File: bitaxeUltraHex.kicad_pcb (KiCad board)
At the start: 4 copper layers, 136.3 x 79.7 mm, 277 parts, among them J1 Conn_01x01, J2 Conn_01x01, J3 Conn_01x04, J4 TC2030-IDC, J5 Conn_01x04, J6 Conn_01x04, Q1 NTMFS5C673NLT1G, Q2 CSD17577Q5A, Q3 NTMFS5C673NLT1G, Q4 CSD17577Q5A, SW1 GT-TC029B-H025-L1N, SW2 GT-TC029B-H025-L1N, U1 uA7805, U10 25MHz, U11 BM1366_mode1, U12 TLV752, U13 MCP1824T-0802E, U14 BM1366_mode1, U15 TMP1075, U16 TMP1075, U17 EMC2302, U18 EMC2101, U19 TLV752, U2 RT9080-33GJ5, U20 MCP1824T-0802E, U21 BM1366_mode1, U22 BM1366_mode1, U23 TLV752, U24 MCP1824T-0802E, U25 BM1366_mode1, U26 BM1366_mode1, U3 INA219AIDCNR, U4 TPS40305, U5 DS4432U+, U6 SN74LVC1T45DBVR, U7 SN74LVC1T45DBVR, U8 SN74LVC1T45DBVR, U9 ESP32-S3-WROOM-1, Y1 32.768kHz

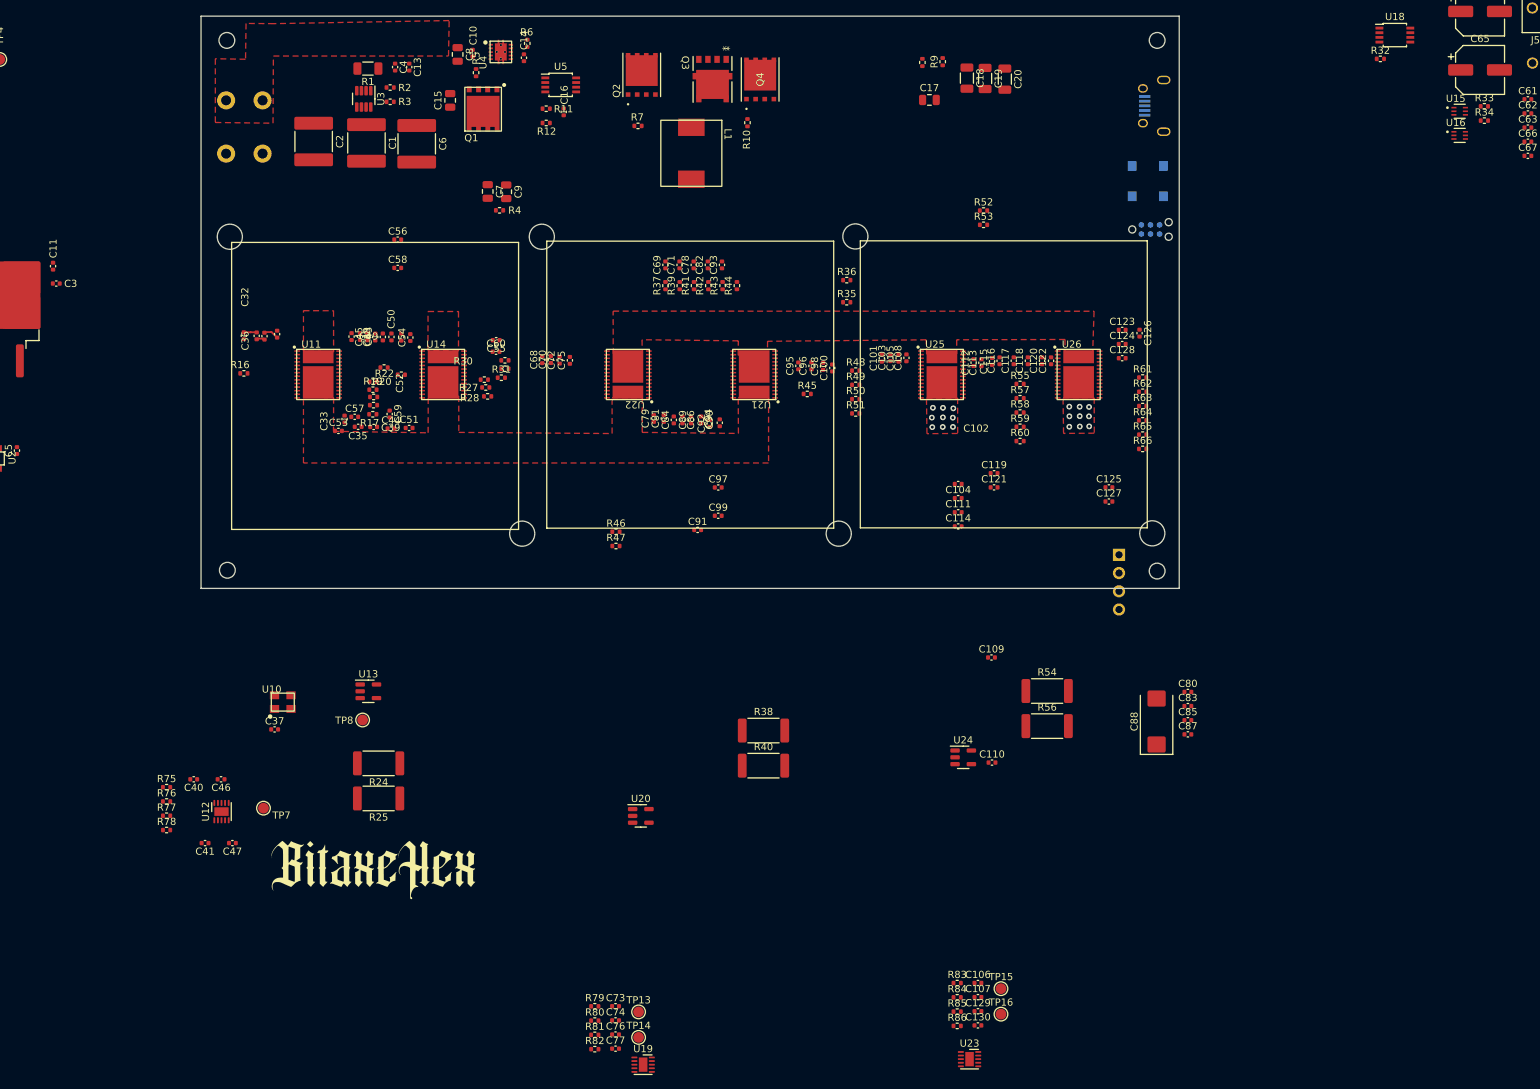
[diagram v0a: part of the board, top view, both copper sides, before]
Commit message: switch voltage reference regulators to ADP170, reannotate
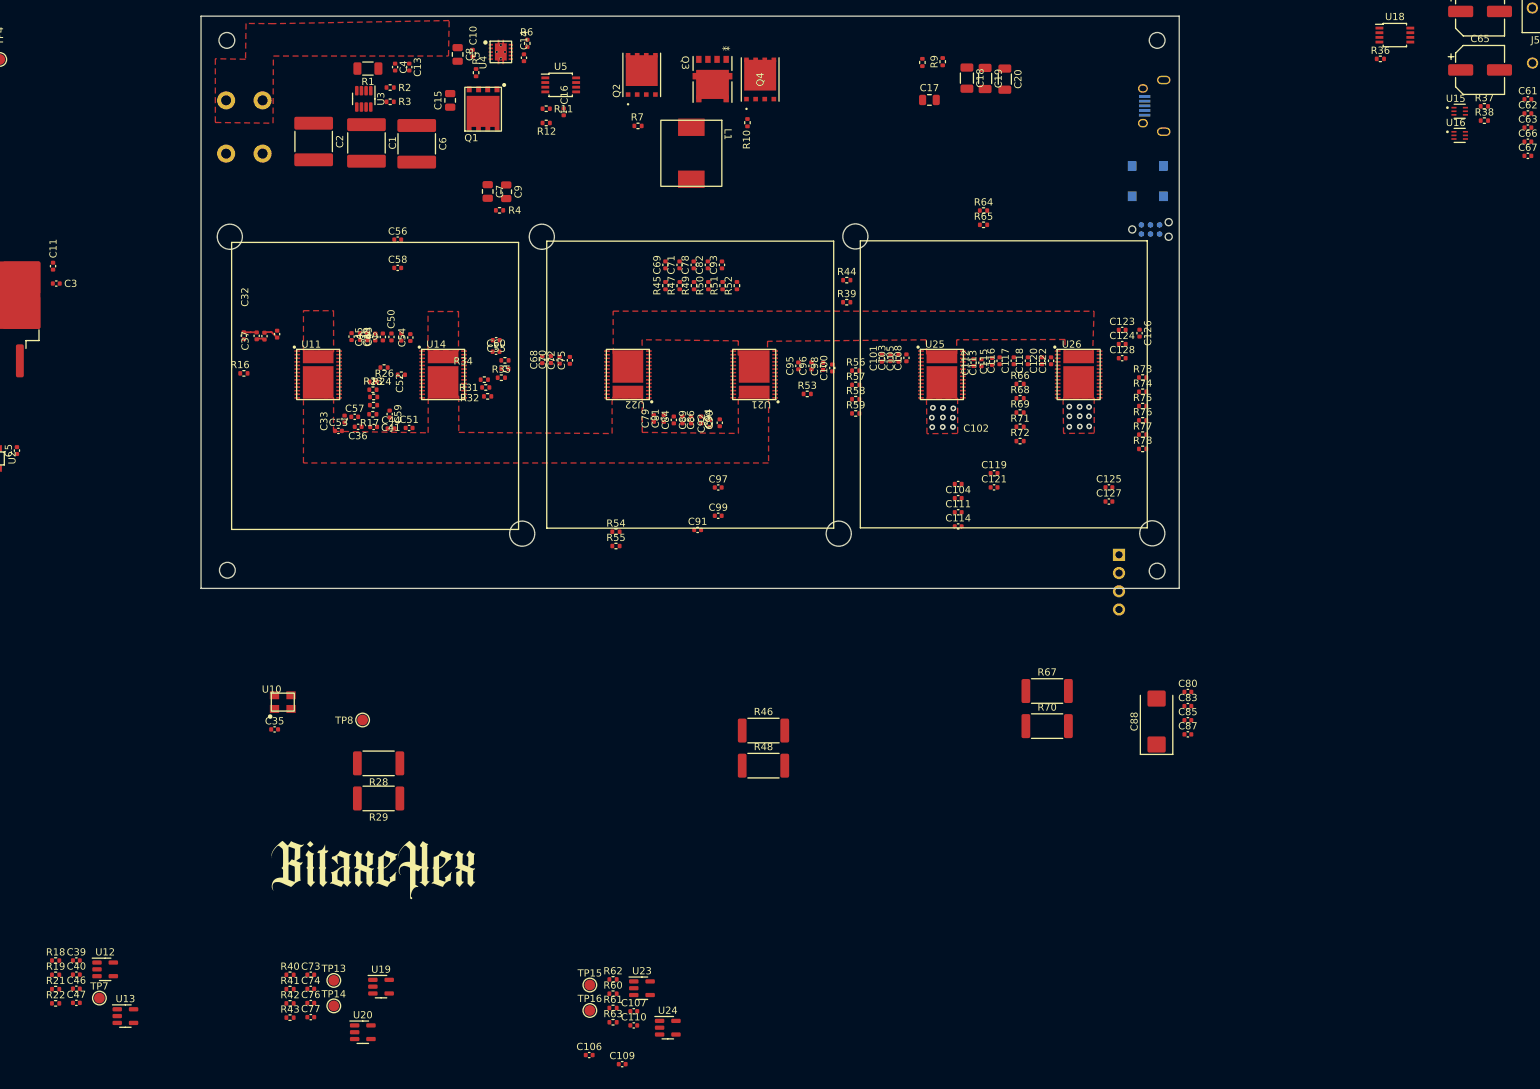
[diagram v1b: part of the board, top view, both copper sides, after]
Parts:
- removed the C106 at (161.8, 182.1)
- removed C129: 0.1uF, Capacitor_SMD:C_0402_1005Metric
- removed C130: 1uF, Capacitor_SMD:C_0402_1005Metric
- removed the C41 at (54.1, 162.6)
- removed the R75 at (48.7, 154.8)
- removed the R76 at (48.7, 156.8)
- removed the R77 at (48.7, 158.8)
- removed the R78 at (48.7, 160.7)
- removed R79, R83: 243K, Resistor_SMD:R_0402_1005Metric
- removed R80, R82, R84, R86: 536K, Resistor_SMD:R_0402_1005Metric
- removed R81, R85: 634K, Resistor_SMD:R_0402_1005Metric
- added C110: 1uF, Capacitor_SMD:C_0402_1005Metric, F.Cu at (113.8, 188.0)
- added C39: 0.1uF, Capacitor_SMD:C_0402_1005Metric, F.Cu at (36.2, 178.9)
- added R18: 309K, Resistor_SMD:R_0402_1005Metric, F.Cu at (33.3, 178.9)
- added R19: 130K, Resistor_SMD:R_0402_1005Metric, F.Cu at (33.3, 180.9)
- added R21: 182K, Resistor_SMD:R_0402_1005Metric, F.Cu at (33.3, 182.9)
- added R22: 182K, Resistor_SMD:R_0402_1005Metric, F.Cu at (33.3, 184.9)
- added R40: 309K, Resistor_SMD:R_0402_1005Metric, F.Cu at (65.9, 180.9)
- added R41: 130K, Resistor_SMD:R_0402_1005Metric, F.Cu at (65.9, 182.9)
- added R42: 182K, Resistor_SMD:R_0402_1005Metric, F.Cu at (65.9, 184.9)
- added R43: 182K, Resistor_SMD:R_0402_1005Metric, F.Cu at (65.9, 186.9)
- added R60: 309K, Resistor_SMD:R_0402_1005Metric, F.Cu at (110.9, 183.5)
- added R61: 130K, Resistor_SMD:R_0402_1005Metric, F.Cu at (110.9, 185.5)
- added R62: 182K, Resistor_SMD:R_0402_1005Metric, F.Cu at (110.9, 181.6)
- added R63: 182K, Resistor_SMD:R_0402_1005Metric, F.Cu at (110.9, 187.5)
- C106: renamed from C110; value 1uF -> 0.1uF
- C107: value 1uF -> 0.1uF
- U12, U19, U23: value TLV752 -> ADP171AUJ-R7; footprint Package_SON:WSON-10-1EP_2.5x2.5mm_P0.5mm_EP1.2x2mm -> Package_TO_SOT_SMD:TSOT-23-5
- U13: renamed from U24; value MCP1824T-0802E -> ADP171AUJ-R7; footprint Package_TO_SOT_SMD:SOT-23-5 -> Package_TO_SOT_SMD:TSOT-23-5
- U20: value MCP1824T-0802E -> ADP171AUJ-R7; footprint Package_TO_SOT_SMD:SOT-23-5 -> Package_TO_SOT_SMD:TSOT-23-5
- U24: renamed from U13; value MCP1824T-0802E -> ADP171AUJ-R7; footprint Package_TO_SOT_SMD:SOT-23-5 -> Package_TO_SOT_SMD:TSOT-23-5
- moved U13 122.2 mm to (43.0, 186.7)
- moved C109 76.5 mm to (112.2, 193.4)
- moved C106 69.4 mm to (107.6, 192.1)
- moved U24 62.7 mm to (118.6, 188.3)
- moved TP15 57.3 mm to (107.7, 182.3)
- moved TP16 57.3 mm to (107.7, 185.9)
- moved U20 49.1 mm to (76.1, 188.9)
- moved C107 48.0 mm to (113.8, 186.0)
- moved U23 46.7 mm to (115.0, 182.8)
- moved C73 42.7 mm to (68.8, 180.9)
- moved C74 42.7 mm to (68.8, 182.9)
- moved C76 42.7 mm to (68.8, 184.8)
- moved C77 42.7 mm to (68.8, 186.8)
- moved TP13 42.7 mm to (72.0, 181.7)
- moved TP14 42.7 mm to (72.0, 185.2)
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- renumbered C37 to C35, C35 to C36, C36 to C37, C39 to C41, R18 to R20, R19 to R23, R20 to R24, R21 to R25, R22 to R26, R23 to R27, R24 to R28, R25 to R29, R26 to R30, R27 to R31, R28 to R32, R29 to R33, R30 to R34, R31 to R35, R32 to R36, R33 to R37, R34 to R38, R35 to R39, R36 to R44, R37 to R45, R38 to R46, R39 to R47, R40 to R48, R41 to R49, R42 to R50, R43 to R51, R44 to R52, R45 to R53, R46 to R54, R47 to R55, R48 to R56, R49 to R57, R50 to R58, R51 to R59, R52 to R64, R53 to R65, R55 to R66, R54 to R67, R57 to R68, R58 to R69, R56 to R70, R59 to R71, R60 to R72, R61 to R73, R62 to R74, R63 to R75, R64 to R76, R65 to R77, R66 to R78
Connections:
- C106 pad 1: /BM1366-3/0V8 -> /5V
- C107 pad 1: /BM1366-3/1V2 -> /5V
- C109 pad 1: /BM1366-3/1V2 -> /BM1366-3/0V8
- U12 pad 1: Net-(U12A-FB1) -> /5V
- U12 pad 4: /FGND2 -> Net-(U12-ADJ)
- U12 pad 5: /5V -> /BM1366-1/0V8
- U13 pad 2: GND -> /FGND2
- U13 pad 4: unconnected-(U24-PG-Pad4) -> Net-(U13-ADJ)
- U13 pad 5: /BM1366-3/0V8 -> /BM1366-1/1V2
- U19 pad 1: Net-(U19A-FB1) -> /5V
- U19 pad 4: /FGND1 -> Net-(U19-ADJ)
- U19 pad 5: /5V -> /BM1366-2/0V8
- U20 pad 2: /BM1366-2/GND -> /FGND1
- U20 pad 4: unconnected-(U20-PG-Pad4) -> Net-(U20-ADJ)
- U20 pad 5: /BM1366-2/0V8 -> /BM1366-2/1V2
- U23 pad 1: Net-(U23A-FB1) -> /5V
- U23 pad 4: GND -> Net-(U23-ADJ)
- U23 pad 5: /5V -> /BM1366-3/0V8
- U24 pad 2: /BM1366-1/GND -> GND
- U24 pad 4: unconnected-(U13-PG-Pad4) -> Net-(U24-ADJ)
- U24 pad 5: /BM1366-1/0V8 -> /BM1366-3/1V2

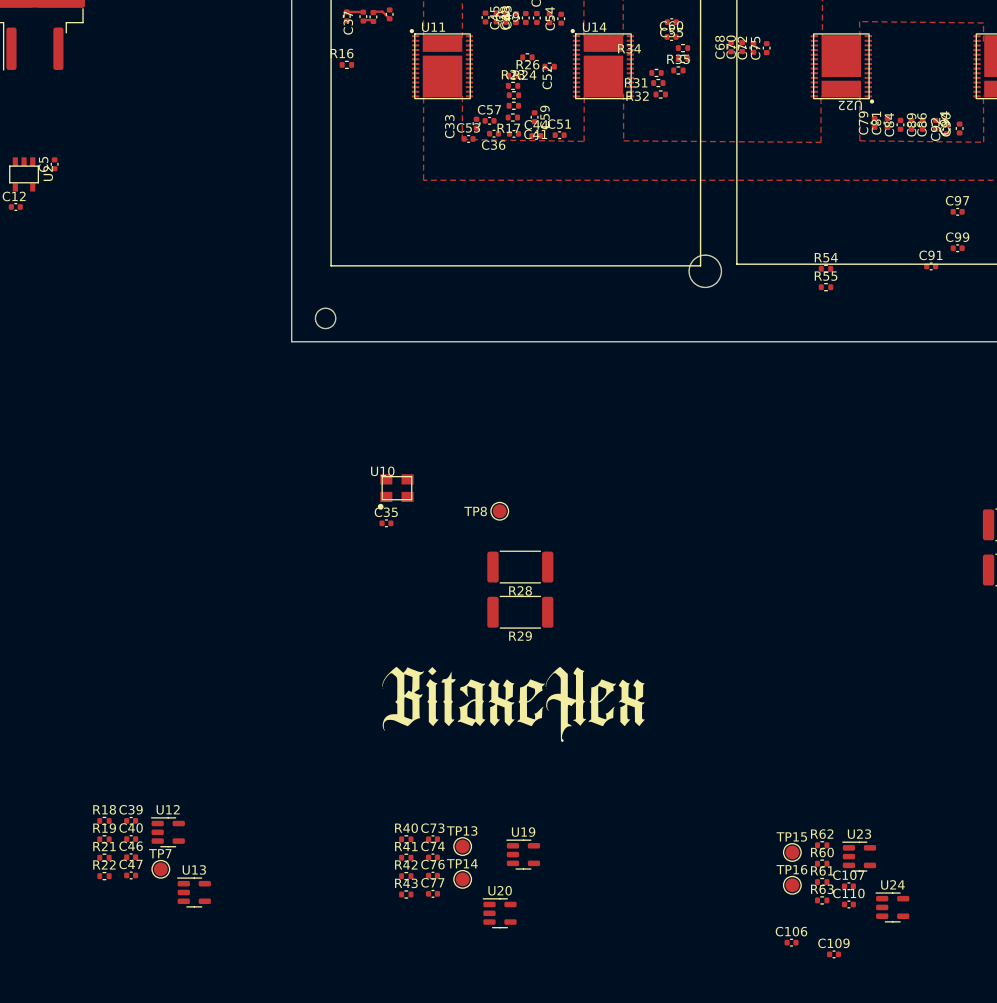
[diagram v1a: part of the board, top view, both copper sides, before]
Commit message: arrange components around voltage regulators
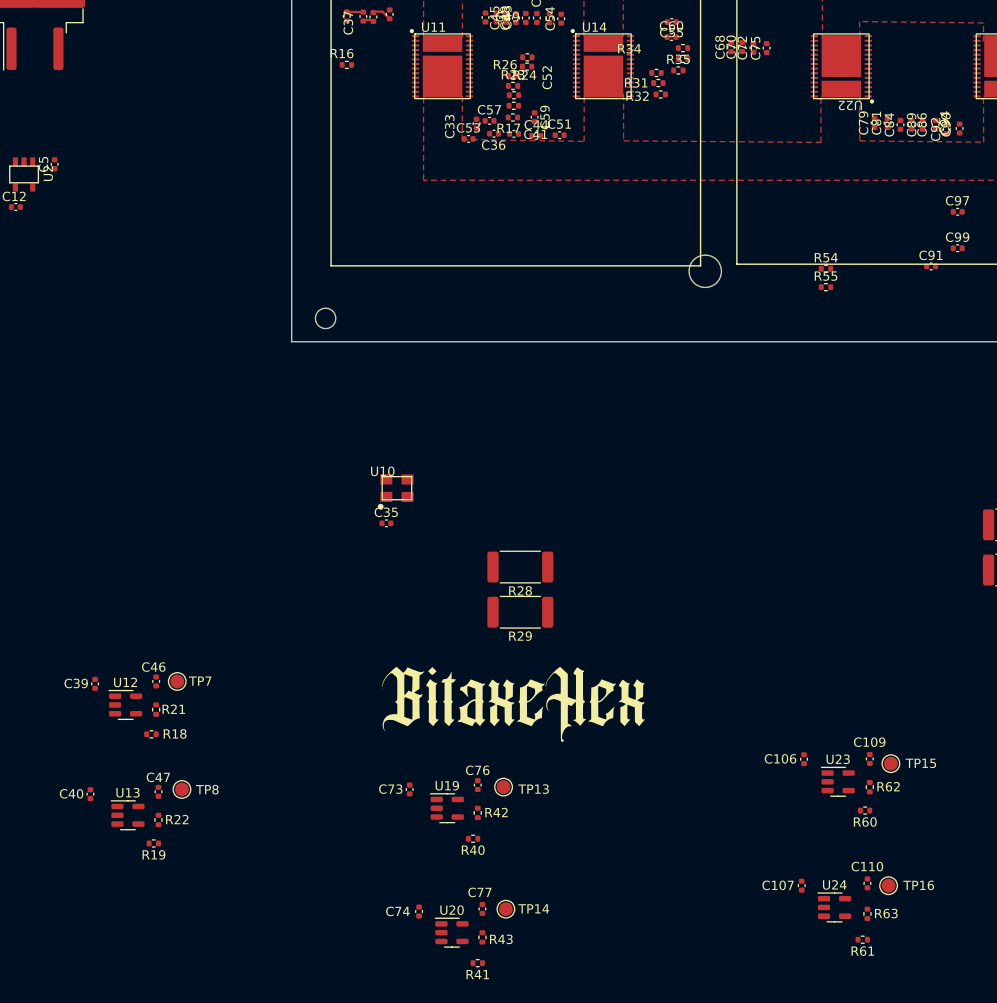
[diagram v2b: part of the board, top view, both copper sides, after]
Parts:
- moved TP8 45.7 mm to (41.7, 175.5)
- moved C109 21.5 mm to (116.1, 172.2), turned to 90 degrees
- moved TP7 20.4 mm to (41.1, 163.8)
- moved C106 19.9 mm to (109.0, 172.2), turned to 90 degrees
- moved C46 19.2 mm to (38.9, 163.8), turned to 90 degrees
- moved R21 17.0 mm to (38.9, 166.9), turned to -90 degrees
- moved C39 15.3 mm to (32.3, 164.1), turned to 90 degrees
- moved U12 14.5 mm to (35.6, 166.4)
- moved TP15 14.4 mm to (118.4, 172.7)
- moved R41 13.8 mm to (73.7, 194.3)
- moved U13 11.0 mm to (35.8, 178.3)
- moved C76 10.9 mm to (73.7, 175.0), turned to 90 degrees
- moved R18 10.7 mm to (38.4, 169.5)
- moved TP16 10.4 mm to (118.1, 185.9)
- moved R42 10.3 mm to (73.7, 178.1), turned to -90 degrees
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
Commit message: Rough draft parts placement
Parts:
- Q3: footprint bitaxe:NTMFS5C673NLT1G -> bitaxe:CSD17311Q5
- U6: moved to F.Cu
- moved C12 113.5 mm to (130.2, 73.1)
- moved C5 113.5 mm to (134.4, 68.5)
- moved U2 113.5 mm to (131.1, 69.6)
- moved U1 111.1 mm to (132.1, 55.4)
- moved C11 107.7 mm to (138.9, 63.5)
- moved C3 94.3 mm to (125.2, 63.5), turned to -90 degrees
- moved TP16 71.5 mm to (177.3, 145.8)
- moved C110 71.2 mm to (174.8, 145.8)
- moved R61 71.2 mm to (174.2, 151.9)
- moved R63 71.2 mm to (174.8, 149.1)
- moved U24 71.2 mm to (171.2, 148.4)
- moved C107 70.4 mm to (167.9, 147.8), turned to -90 degrees
- moved C77 70.3 mm to (128.4, 143.7)
- moved R41 70.3 mm to (127.9, 149.6)
- moved U20 70.3 mm to (125.1, 146.3)
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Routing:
- added copper zone on F.Cu, net /Power/VIN
- removed copper zone on F.Cu, net /Power/VIN_M

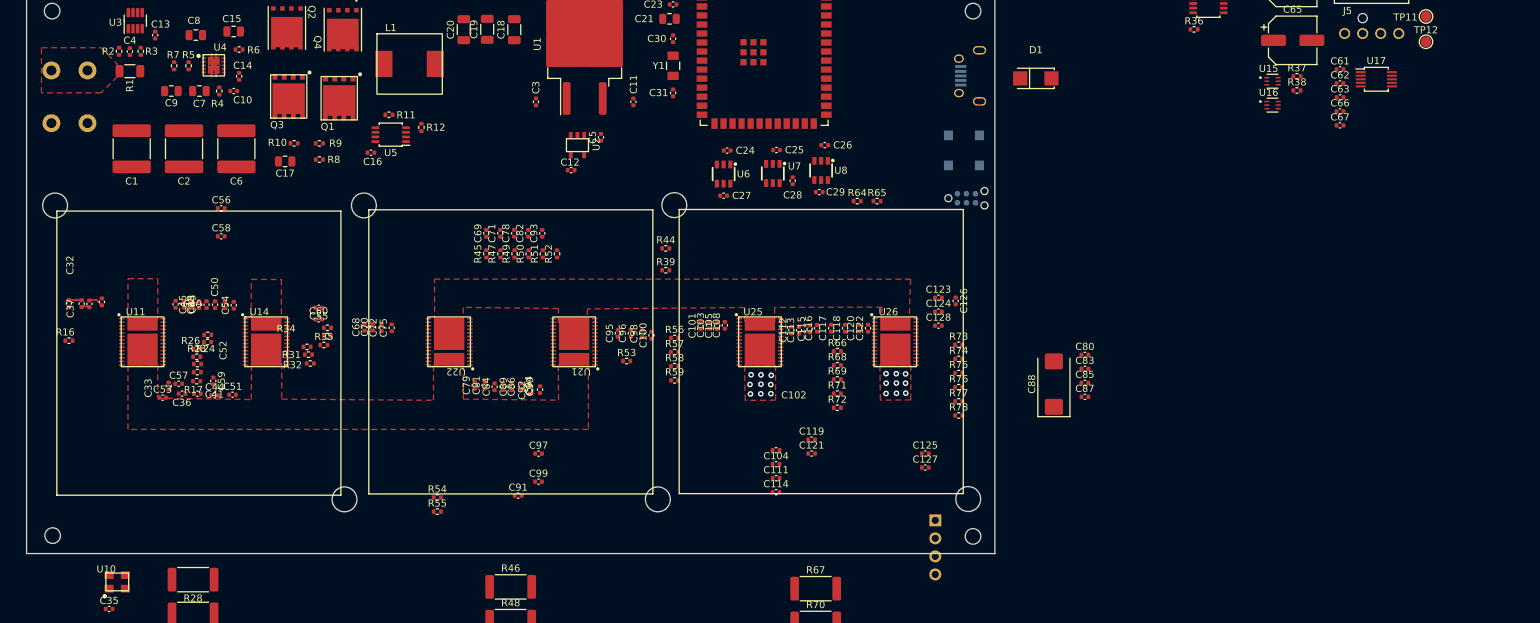
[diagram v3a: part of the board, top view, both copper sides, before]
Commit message: changed USB connector to USB C. updated display.
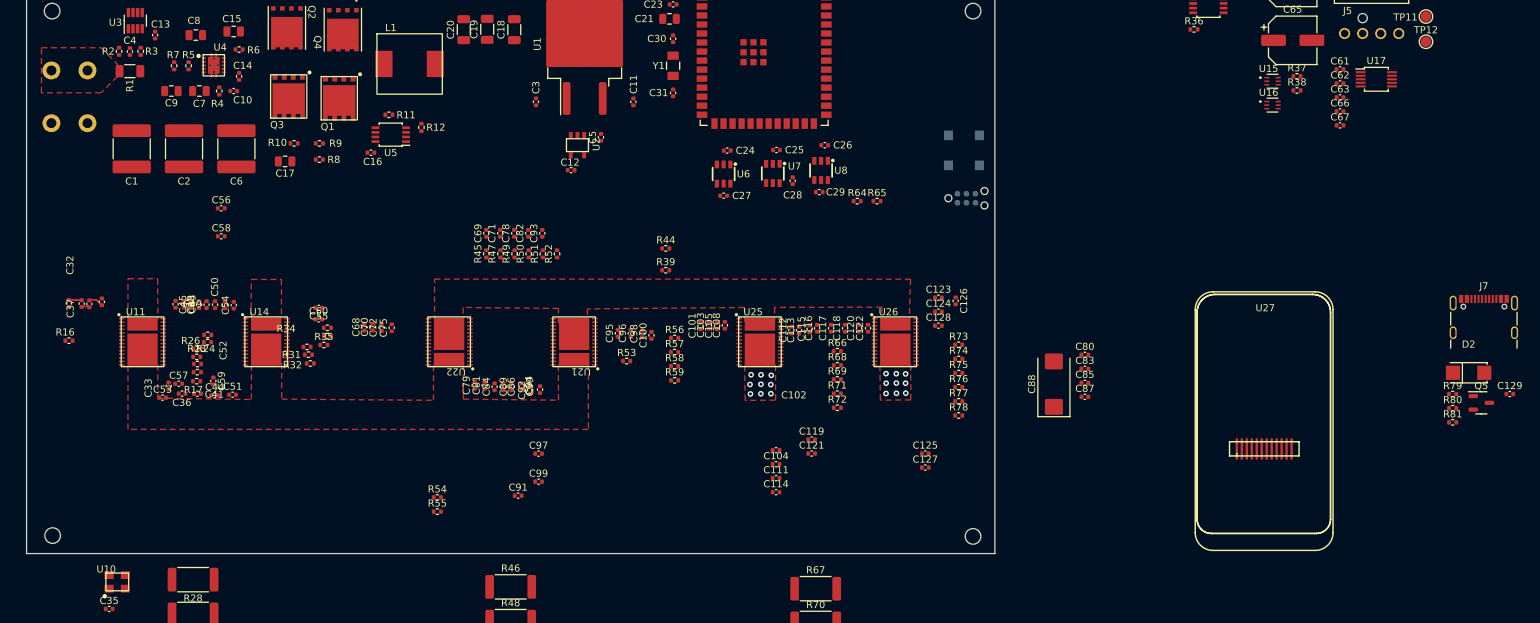
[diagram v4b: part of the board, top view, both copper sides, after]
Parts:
- removed D1: SS310_C85658, bitaxe:SMA_L4.3-W2.6-LS5.2-RD
- removed H10, H5, H6, H7, H8, H9: MountingHole, MountingHole:MountingHole_3.5mm
- removed J3: Conn_01x04, Connector_PinHeader_2.54mm:PinHeader_1x04_P2.54mm_Vertical
- removed USB1: U254-051T-4BHJ25-F2S, bitaxe:MICRO-USB-SMD_U254-051T-4BHJ25-F2S
- added C129: 0.1uF, Capacitor_SMD:C_0402_1005Metric, F.Cu at (262.3, 104.6)
- added D2: SS310, lcsc:SMA_L4.3-W2.6-LS5.2-RD, F.Cu at (256.5, 101.6)
- added J7: USB_C_Receptacle_USB2.0, Connector_USB:USB_C_Receptacle_GCT_USB4105-xx-A_16P_TopMnt_Horizontal, F.Cu at (258.6, 94.9)
- added Q5: S8050, Package_TO_SOT_SMD:SOT-23-3, F.Cu at (258.3, 105.9)
- added R79: 5.1k, Resistor_SMD:R_0402_1005Metric, F.Cu at (254.2, 104.6)
- added R80: 5.1k, Resistor_SMD:R_0402_1005Metric, F.Cu at (254.2, 106.6)
- added R81: 10, Resistor_SMD:R_0402_1005Metric, F.Cu at (254.2, 108.6)
- added U27: 176x320_st7789, bitaxe:ST7789-176x320, F.Cu at (252.0, 138.0)
- R15: value 1k -> 10k
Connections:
- R14 pad 1: /SCL -> /ESP32/TFT_BLK
- R14 pad 2: /3V3 -> Net-(Q5-B)
- R15 pad 1: /SDA -> Net-(Q5-B)
- U9 pad 12: unconnected-(U9-GPIO8/TOUCH8/ADC1_CH7/SUBSPICS1-Pad12) -> /ESP32/TFT_DC
- U9 pad 15: Net-(U9-GPIO3/TOUCH3/ADC1_CH2*) -> /3V3
- U9 pad 17: unconnected-(U9-GPIO9/TOUCH9/ADC1_CH8/FSPIHD/SUBSPIHD-Pad17) -> /ESP32/TFT_BLK
- U9 pad 4: unconnected-(U9-GPIO4/TOUCH4/ADC1_CH3-Pad4) -> /ESP32/TFT_RES
- U9 pad 5: unconnected-(U9-GPIO5/TOUCH5/ADC1_CH4-Pad5) -> /ESP32/TFT_SDA
- U9 pad 6: unconnected-(U9-GPIO6/TOUCH6/ADC1_CH5-Pad6) -> /ESP32/TFT_SCL
- U9 pad 7: unconnected-(U9-GPIO7/TOUCH7/ADC1_CH6-Pad7) -> /ESP32/TFT_CS
